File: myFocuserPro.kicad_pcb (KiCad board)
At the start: 2 copper layers, 70 x 50 mm, 41 parts, among them J1 PB1, J10 PWR_LED, J11 PPTC, J12 BT, J13 STEPPER, J14 HPSW, J15 PWR_SW, J2 PB2, J3 PRG, J4 BLED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

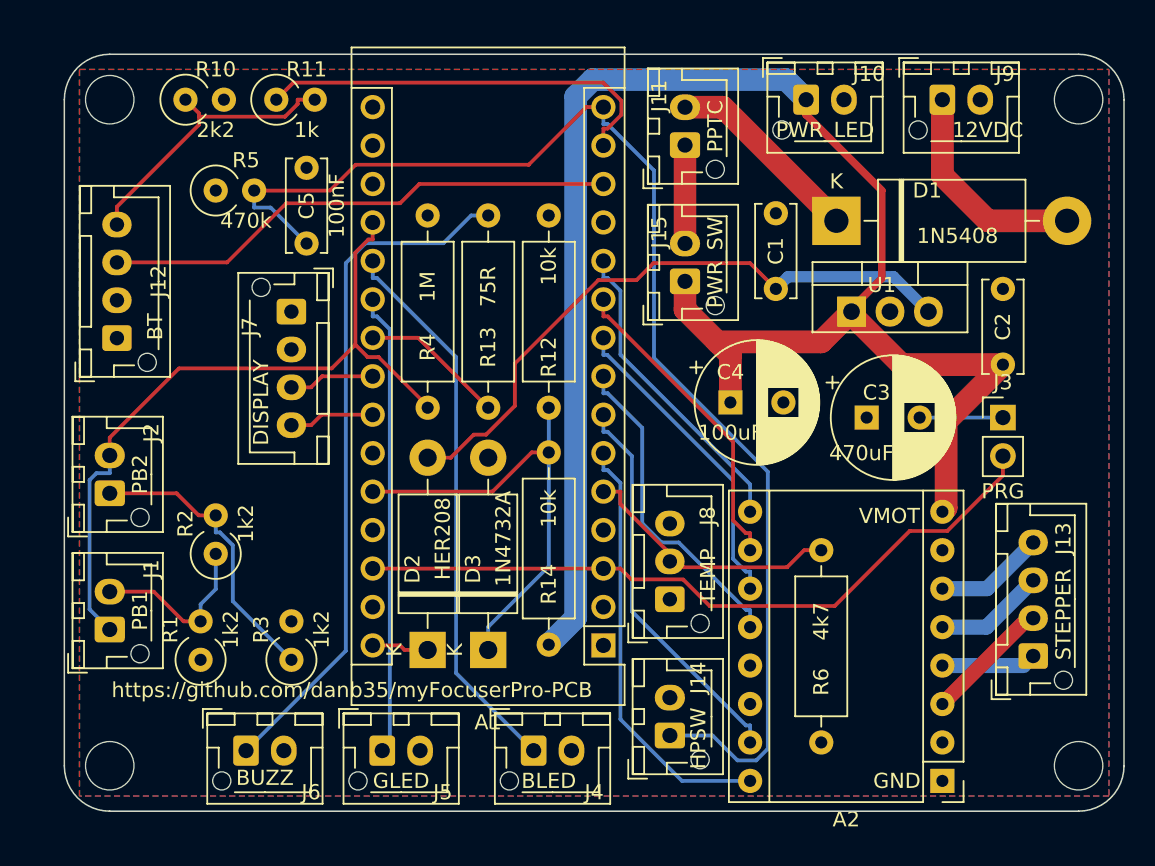
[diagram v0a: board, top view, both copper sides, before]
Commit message: Update JST footprints
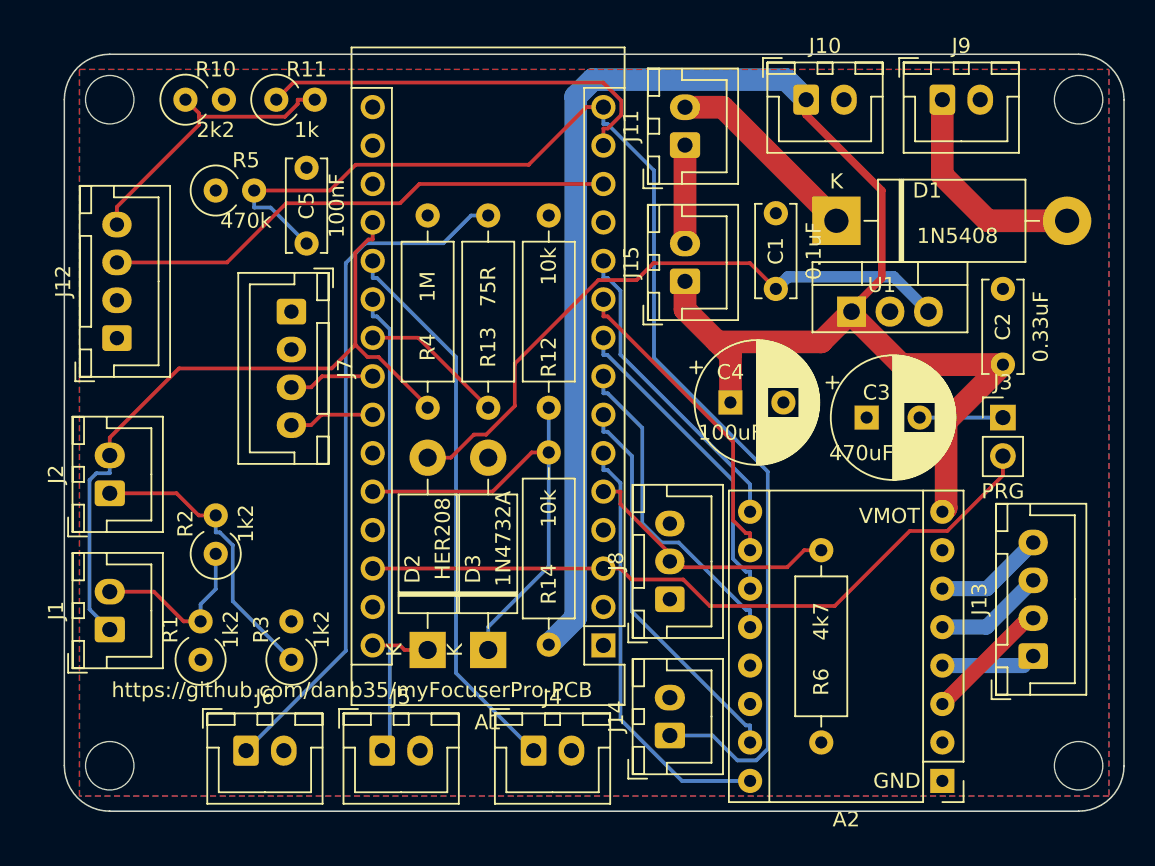
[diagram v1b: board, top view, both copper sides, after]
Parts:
- J1, J10, J11, J14, J15, J2, J4, J5, J6, J9: footprint Connector_JST:JST_XH_B2B-XH-AM_1x02_P2.50mm_Vertical -> Connector_JST:JST_XH_B2B-XH-A_1x02_P2.50mm_Vertical
- J12, J13, J7: footprint Connector_JST:JST_XH_B4B-XH-AM_1x04_P2.50mm_Vertical -> Connector_JST:JST_XH_B4B-XH-A_1x04_P2.50mm_Vertical
- J8: footprint Connector_JST:JST_XH_B3B-XH-AM_1x03_P2.50mm_Vertical -> Connector_JST:JST_XH_B3B-XH-A_1x03_P2.50mm_Vertical

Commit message: Connect isolated grounds
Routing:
- net GND: track 0.00 -> 60.0 mm, vias 0 -> 1
- net +5V: track 0.00 -> 22.1 mm, vias 0 -> 2
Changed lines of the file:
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@@
   (segment (start 60.37 133.97) (end 75.61 133.97) (width 0.25) (layer "F.Cu") (net 3))
   (segment (start 102 127.8184) (end 102 126.54) (width 0.25) (layer "F.Cu") (net 3))
+  (segment (start 55.95 136.51) (end 55 137.46) (width 0.25) (layer "F.Cu") (net 4))
+  (segment (start 69.474511 125.175489) (end 68 126.65) (width 0.25) (layer "F.Cu") (net 4))
+  (segment (start 80 129.1497) (end 76.025789 125.175489) (width 0.25) (layer "F.Cu") (net 4))
+  (segment (start 80 131) (end 80 129.1497) (width 0.25) (layer "F.Cu") (net 4))
+  (segment (start 75.61 131.43) (end 69.43 131.43) (width 0.25) (layer "F.Cu") (net 4))
+  (segment (start 69.43 131.43) (end 68 130) (width 0.25) (layer "F.Cu") (net 4))
+  (segment (start 60.37 136.51) (end 55.95 136.51) (width 0.25) (layer "F.Cu") (net 4))
+  (segment (start 76.025789 125.175489) (end 69.474511 125.175489) (width 0.25) (layer "F.Cu") (net 4))
+  (via (at 68 130) (size 0.8) (drill 0.4) (layers "F.Cu" "B.Cu") (net 4))
+  (segment (start 98 148) (end 96.5 149.5) (width 0.25) (layer "B.Cu") (net 4))
+  (segment (start 68 130) (end 68 126.65) (width 0.25) (layer "B.Cu") (net 4))
+  (segment (start 77 149.5) (end 73.5 146) (width 0.25) (layer "B.Cu") (net 4))
+  (segment (start 96.5 149.5) (end 77 149.5) (width 0.25) (layer "B.Cu") (net 4))
   (segment (start 87.7494 133.8853) (end 88.8747 132.76) (width 0.25) (layer "F.Cu") (net 5))
   (segment (start 76.7353 128.89) (end 76.7353 129.7196) (width 0.25) (layer "F.Cu") (net 5))
@@
   (segment (start 72 133.8247) (end 68 137.8247) (width 0.25) (layer "B.Cu") (net 26))
   (segment (start 72 126.3) (end 72 133.8247) (width 0.25) (layer "B.Cu") (net 26))
+  (segment (start 93 124) (end 93 131.5) (width 0.25) (layer "F.Cu") (net 27))
+  (segment (start 89.62 140.38) (end 85.3 140.38) (width 0.25) (layer "F.Cu") (net 27))
+  (segment (start 93 137) (end 89.62 140.38) (width 0.25) (layer "F.Cu") (net 27))
+  (via (at 93 131.5) (size 0.8) (drill 0.4) (layers "F.Cu" "B.Cu") (net 27))
+  (via (at 93 137) (size 0.8) (drill 0.4) (layers "F.Cu" "B.Cu") (net 27))
+  (segment (start 93 131.5) (end 93 137) (width 0.25) (layer "B.Cu") (net 27))
   (segment (start 62.1747 139.05) (end 62.4747 139.35) (width 0.25) (layer "F.Cu") (net 28))
   (segment (start 64 139.35) (end 62.4747 139.35) (width 0.25) (layer "F.Cu") (net 28))

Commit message: Update PCB layout
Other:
- board text added: "M-MT-F-BT DRV8825-HW203 myFocuserPro2 Rev13 (c) R Brown 2017 (c) D Brown 2022"
- board text removed: "M-MT-F-BT DRV8825-HW203 myFocuserPro2 Rev12 (c) R Brown 2017 (c) D Brown 2022"
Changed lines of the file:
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@@
     (property "Sheetname" "")
     (attr through_hole)
-    (fp_text reference "C2" (at 2.5 0 90) (layer "F.SilkS")
-      (effects (font (size 1 1) (thickness 0.15)))
-    )
-    (fp_text value "0.33uF" (at 2.5 2.5 90) (layer "F.SilkS")
-      (effects (font (size 1 1) (thickness 0.15)))
-    )
-    (fp_text user "${REFERENCE}" (at 2.5 0 90) (layer "F.Fab")
+    (fp_text reference "C2" (at 2.5 -0.5 90) (layer "F.SilkS")
+      (effects (font (size 1 1) (thickness 0.15)))
+    )
+    (fp_text value "0.33uF" (at 2 1 90) (layer "F.SilkS")
+      (effects (font (size 1 1) (thickness 0.15)))
+    )
+    (fp_text user "${REFERENCE}" (at 2.5 -0.5 90) (layer "F.Fab")
       (effects (font (size 1 1) (thickness 0.15)))
     )
@@
     (property "Sheetname" "")
     (attr through_hole)
-    (fp_text reference "C1" (at 2.5 0 90) (layer "F.SilkS")
-      (effects (font (size 1 1) (thickness 0.15)))
-    )
-    (fp_text value "0.1uF" (at 2.5 2.5 90) (layer "F.SilkS")
-      (effects (font (size 1 1) (thickness 0.15)))
-    )
-    (fp_text user "${REFERENCE}" (at 2.5 0 90) (layer "F.Fab")
+    (fp_text reference "C1" (at 2.5 -0.5 90) (layer "F.SilkS")
+      (effects (font (size 1 1) (thickness 0.15)))
+    )
+    (fp_text value "0.1uF" (at 2.5 1 90) (layer "F.SilkS")
+      (effects (font (size 1 1) (thickness 0.15)))
+    )
+    (fp_text user "${REFERENCE}" (at 2.5 -0.5 90) (layer "F.Fab")
       (effects (font (size 1 1) (thickness 0.15)))
     )
@@
     (effects (font (size 1 1) (thickness 0.15)) (justify mirror))
   )
-  (gr_text "M-MT-F-BT  DRV8825-HW203\nmyFocuserPro2 Rev12\n(c) R Brown 2017\n(c) D Brown 2022" (at 93.5 137.5 270) (layer "B.SilkS")
+  (gr_text "M-MT-F-BT  DRV8825-HW203\nmyFocuserPro2 Rev13\n(c) R Brown 2017\n(c) D Brown 2022" (at 93.5 137.5 270) (layer "B.SilkS")
     (effects (font (size 1 1) (thickness 0.15)) (justify mirror))
   )
